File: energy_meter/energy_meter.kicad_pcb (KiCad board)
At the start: 2 copper layers, 120 x 115 mm, 125 parts, among them IC1 ADUM4151BRIZ, IC2 ADUM6404ARIZ, IC3 ADP122AUJZ-3.3-R7, IC4 24LC32A_SN, J1 Screw_Terminal_01x02, J10 IB_in, J2 Screw_Terminal_01x02, J3 MicroUSB, J8 5V_SMPS, J9 IA_in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

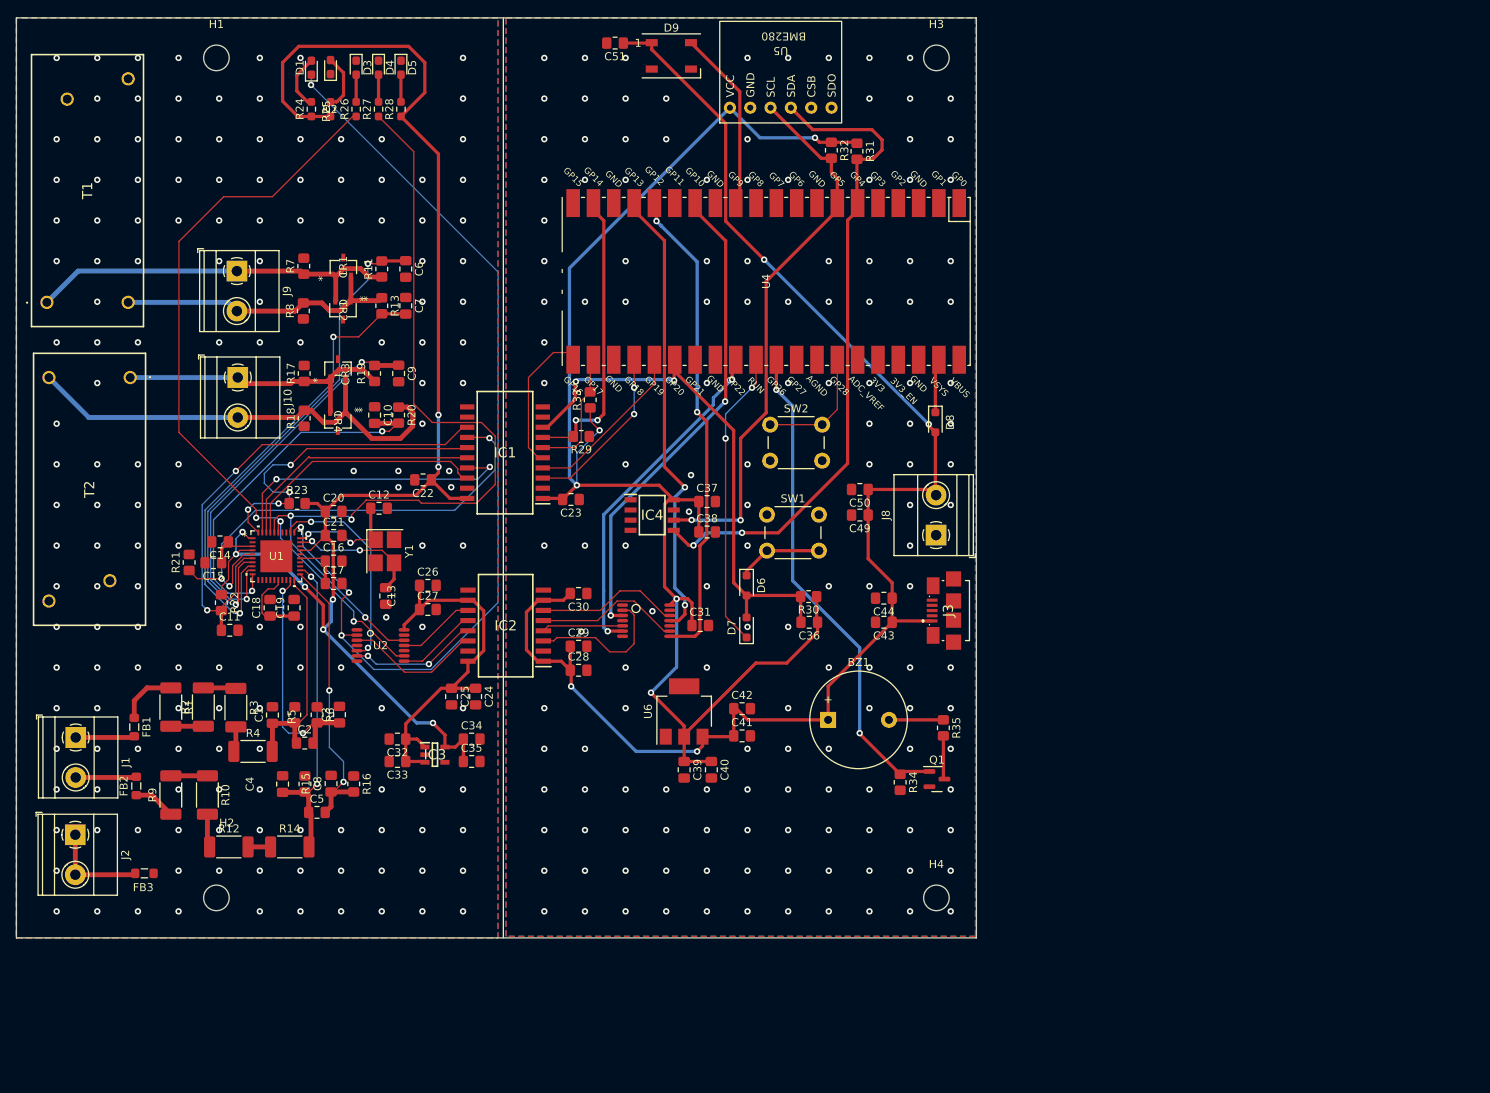
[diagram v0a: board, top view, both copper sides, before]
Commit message: Silkscreen done
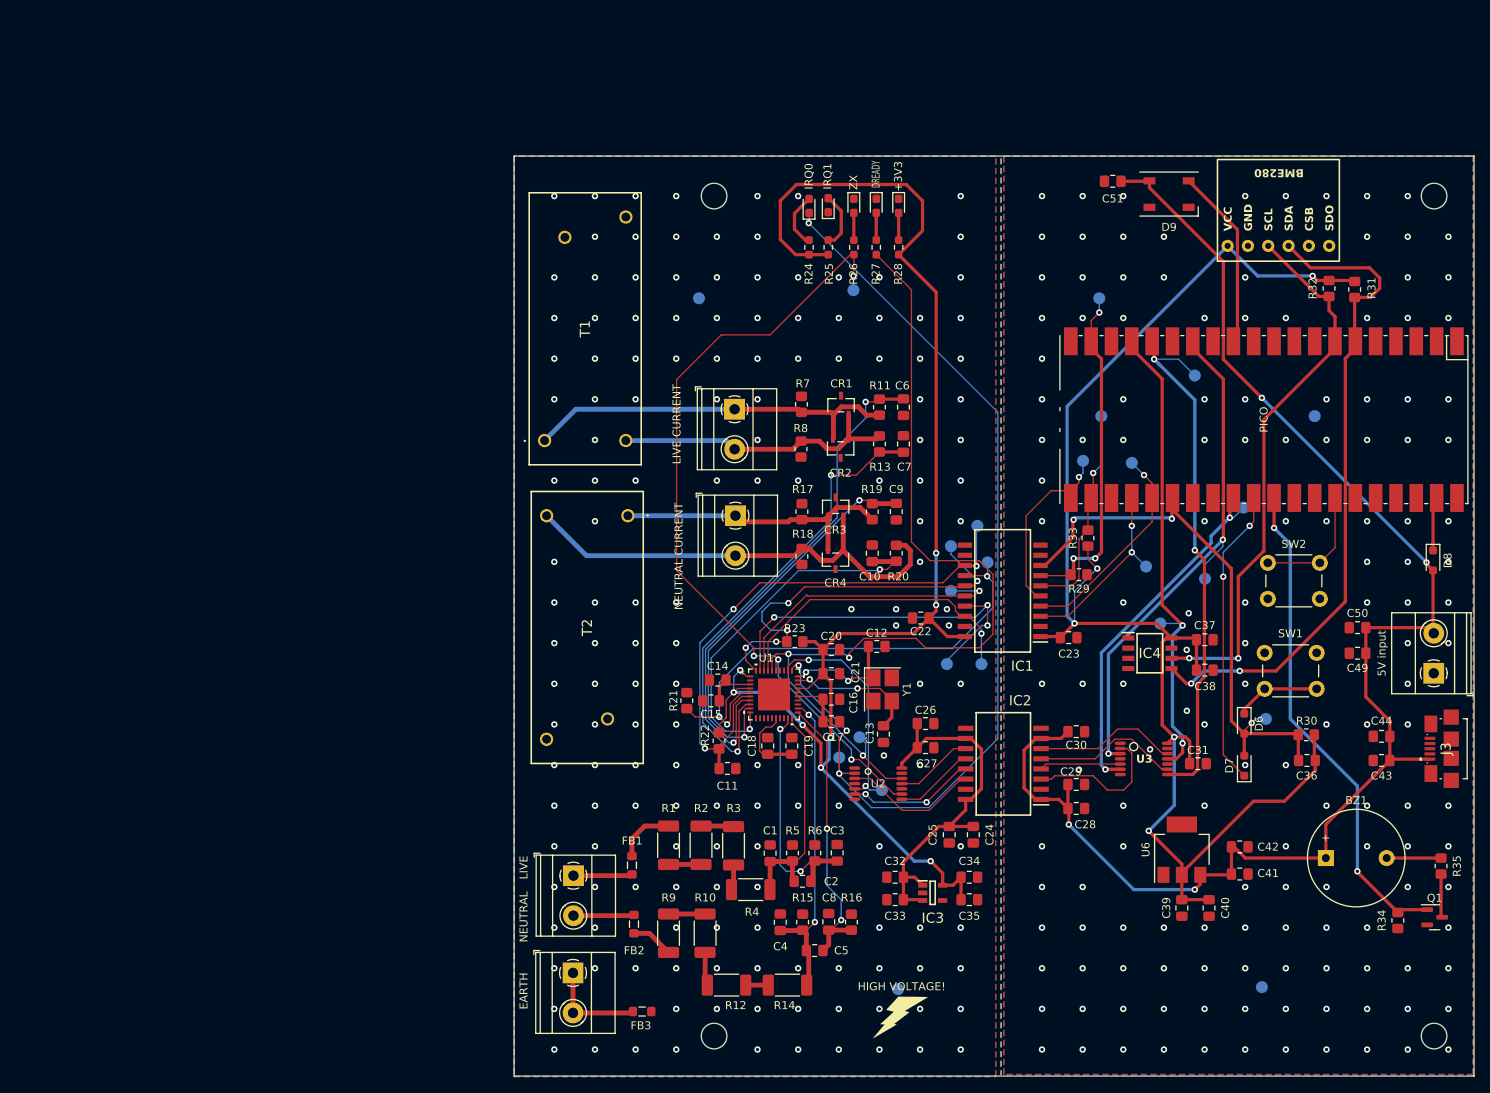
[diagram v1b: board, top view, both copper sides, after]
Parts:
- added DREADY_ADE: TestPoint, TestPoint:TestPoint_Pad_D1.5mm, B.Cu at (129.5, 109.0)
- added DREADY_ISO: TestPoint, TestPoint:TestPoint_Pad_D1.5mm, B.Cu at (167.1, 94.7)
- added G***: LOGO, bitmaps:lightning, F.Cu at (134.6, 144.0)
- added GND: TestPoint, TestPoint:TestPoint_Pad_D1.5mm, B.Cu at (134.3, 140.5)
- added GND: TestPoint, TestPoint:TestPoint_Pad_D1.5mm, B.Cu at (109.5, 54.1)
- added GNDA: TestPoint, TestPoint:TestPoint_Pad_D1.5mm, B.Cu at (179.8, 140.2)
- added GNDA: TestPoint, TestPoint:TestPoint_Pad_D1.5mm, B.Cu at (186.4, 68.8)
- added IRQ0_ADE: TestPoint, TestPoint:TestPoint_Pad_D1.5mm, B.Cu at (127.0, 111.5)
- added IRQ0_ISO: TestPoint, TestPoint:TestPoint_Pad_D1.5mm, B.Cu at (172.7, 89.2)
- added IRQ1_ADE: TestPoint, TestPoint:TestPoint_Pad_D1.5mm, B.Cu at (132.3, 115.6)
- added IRQ1_ISO: TestPoint, TestPoint:TestPoint_Pad_D1.5mm, B.Cu at (177.5, 80.3)
- added MISO_ADE: TestPoint, TestPoint:TestPoint_Pad_D1.5mm, B.Cu at (141.0, 90.7)
- added MISO_ISO: TestPoint, TestPoint:TestPoint_Pad_D1.5mm, B.Cu at (157.5, 74.4)
- added MOSI_ADE: TestPoint, TestPoint:TestPoint_Pad_D1.5mm, B.Cu at (140.4, 99.8)
- added MOSI_ISO: TestPoint, TestPoint:TestPoint_Pad_D1.5mm, B.Cu at (163.6, 74.7)
- added PM1_ADE: TestPoint, TestPoint:TestPoint_Pad_D1.5mm, B.Cu at (145.5, 87.1)
- added PM1_ISO: TestPoint, TestPoint:TestPoint_Pad_D1.5mm, B.Cu at (159.5, 54.1)
- added RESET_ADE: TestPoint, TestPoint:TestPoint_Pad_D1.5mm, B.Cu at (144.3, 82.5)
- added RESET_ISO: TestPoint, TestPoint:TestPoint_Pad_D1.5mm, B.Cu at (180.3, 106.7)
- added SCLK_ADE: TestPoint, TestPoint:TestPoint_Pad_D1.5mm, B.Cu at (144.8, 99.8)
- added SCLK_ISO: TestPoint, TestPoint:TestPoint_Pad_D1.5mm, B.Cu at (165.3, 87.6)
- added SS_ADE: TestPoint, TestPoint:TestPoint_Pad_D1.5mm, B.Cu at (141.0, 85.1)
- added SS_ISO: TestPoint, TestPoint:TestPoint_Pad_D1.5mm, B.Cu at (159.7, 68.8)
- added ZX_ADE: TestPoint, TestPoint:TestPoint_Pad_D1.5mm, B.Cu at (128.8, 53.1)
- added ZX_ISO: TestPoint, TestPoint:TestPoint_Pad_D1.5mm, B.Cu at (171.4, 63.8)
- 5V input: renamed from J8
- LIVE CURRENT: renamed from J9
- NEUTRAL CURRENT: renamed from J10
- moved 5V input 64.6 mm to (201.3, 101.0)
- moved BZ1 64.6 mm to (187.8, 124.1)
- moved C10 64.6 mm to (131.1, 86.0)
- moved C25 64.6 mm to (140.7, 121.2)
- moved C26 64.6 mm to (137.8, 107.3)
- moved C27 64.6 mm to (137.8, 110.3)
- moved C34 64.6 mm to (143.2, 126.5)
- moved C35 64.6 mm to (143.2, 129.3)
- moved C39 64.6 mm to (169.8, 130.3)
- moved C40 64.6 mm to (173.2, 130.3)
- moved C43 64.6 mm to (194.8, 111.9)
- moved C44 64.6 mm to (194.8, 108.9)
- moved C49 64.6 mm to (191.8, 98.5)
- moved C50 64.6 mm to (191.8, 95.3)
- moved C9 64.6 mm to (134.1, 80.8)
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- renumbered D5 to +3V3, D4 to DREADY, D1 to IRQ0, D2 to IRQ1, U4 to PICO, D3 to ZX
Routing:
- net MOSI_ADE: track 37.6 -> 47.5 mm, vias 2 -> 3
- net SS_ISO: track 16.8 -> 26.7 mm, vias 0 -> 1
- net SS_ADE: track 41.8 -> 49.3 mm, vias 4 -> 5
- net SCLK_ADE: track 31.6 -> 38.7 mm, vias 0 -> 1
- net PM1_ISO: track 35.8 -> 42.5 mm, vias 2 -> 3
- net RESET_ADE: track 63.6 -> 70.2 mm, vias 2 -> 3
- net ZX_ISO: track 60.1 -> 66.0 mm
- net IRQ0_ISO: track 59.7 -> 65.5 mm
- net MISO_ADE: track 31.5 -> 37.1 mm, vias 0 -> 1
- net MOSI_ISO: track 22.2 -> 26.7 mm, vias 0 -> 1
- net ZX_ADE: track 96.4 -> 100.9 mm, vias 3 -> 4
- net MISO_ISO: track 17.9 -> 22.3 mm, vias 0 -> 1
- net DREADY_ADE: track 110.4 -> 114.2 mm
- net RESET_ISO: track 72.1 -> 75.8 mm, vias 2 -> 3
- net SCLK_ISO: track 22.4 -> 25.3 mm
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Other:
- board text added: "EARTH"
- board text added: "HIGH VOLTAGE!"
- board text added: "LIVE"
- board text added: "NEUTRAL"
- board text added: "U3"

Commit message: Add bitmaps
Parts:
- removed the G*** at (134.6, 144.0)
- added G***: LOGO, bitmaps:caution_triangle, F.Cu at (134.6, 144.0)
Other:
- board text removed: "HIGH VOLTAGE!"

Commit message: Major progress
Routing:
- net SCL_PICO: track 69.1 -> 71.5 mm
- net BUZZER: track 62.9 -> 64.9 mm
- net SDA_PICO: track 83.3 -> 84.6 mm
- net Net-(FB2-Pad1): track 5.30 -> 6.09 mm
- net DREADY_ADE: track 114.2 -> 114.8 mm
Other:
- board text added: "A&S"
